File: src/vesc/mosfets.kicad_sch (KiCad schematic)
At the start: 50 parts, among them Q1 NCEP60T20, Q2 NCEP60T20, Q3 NCEP60T20, Q4 NCEP60T20, Q5 NCEP60T20, Q6 NCEP60T20

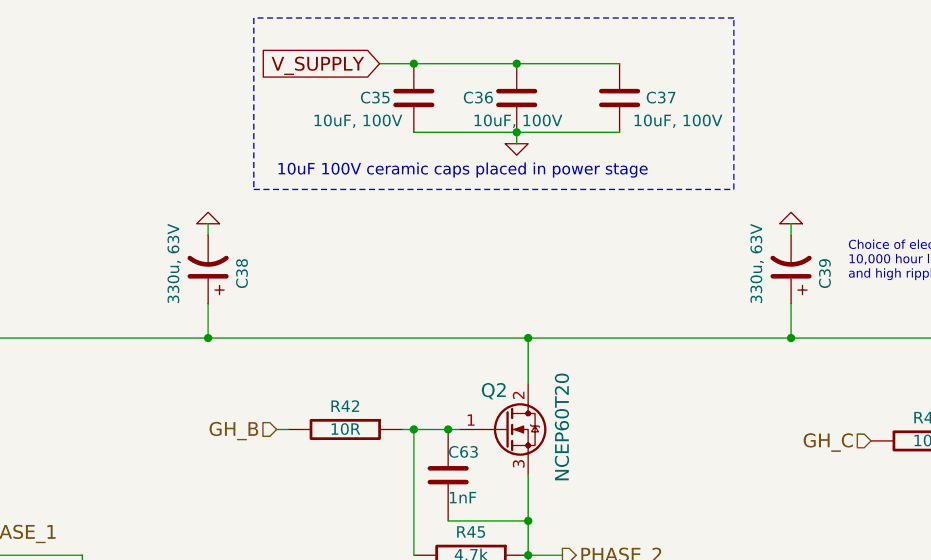
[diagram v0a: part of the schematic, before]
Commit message: replaced 330u electrolytic caps with 270u
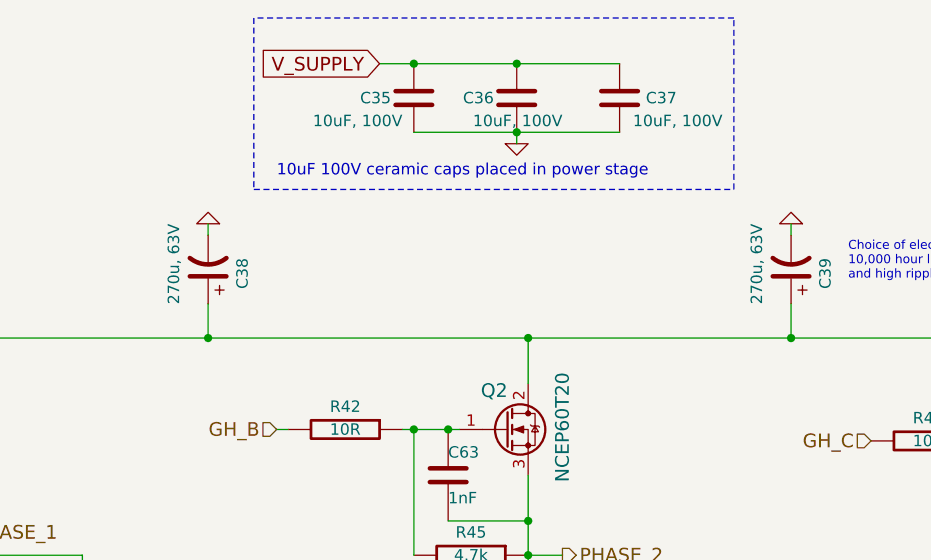
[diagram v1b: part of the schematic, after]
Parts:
- C38, C39: value 330u, 63V -> 270u, 63V
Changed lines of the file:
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@@
 			)
 		)
-		(property "Value" "330u, 63V"
+		(property "Value" "270u, 63V"
 			(at 123.19 58.42 90)
 			(effects
@@
 			)
 		)
-		(property "Value" "330u, 63V"
+		(property "Value" "270u, 63V"
 			(at 187.96 58.42 90)
 			(effects

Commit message: changed power MOSFET capacitor ratings
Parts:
- C35, C36, C37: value 10uF, 100V -> 10uF, 50V
- C40, C41, C42: value 4.7nF, 100V -> 4.7nF, 50V
- C61, C62, C63, C65, C66, C67: value 1nF -> 1nF, 50V
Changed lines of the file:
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@@
 			)
 		)
-		(property "Value" "10uF, 100V"
+		(property "Value" "10uF, 50V"
 			(at 166.37 46.99 0)
 			(effects
@@
 			)
 		)
-		(property "Value" "10uF, 100V"
+		(property "Value" "10uF, 50V"
 			(at 148.59 46.99 0)
 			(effects
@@
 			)
 		)
-		(property "Value" "4.7nF, 100V"
+		(property "Value" "4.7nF, 50V"
 			(at 106.68 107.95 0)
 			(effects
@@
 			)
 		)
-		(property "Value" "4.7nF, 100V"
+		(property "Value" "4.7nF, 50V"
 			(at 172.72 109.22 0)
 			(effects
@@
 			)
 		)
-		(property "Value" "4.7nF, 100V"
+		(property "Value" "4.7nF, 50V"
 			(at 246.38 110.49 0)
 			(effects
@@
 			)
 		)
-		(property "Value" "10uF, 100V"
+		(property "Value" "10uF, 50V"
 			(at 184.15 46.99 0)
 			(effects
@@
 			)
 		)
-		(property "Value" "1nF"
+		(property "Value" "1nF, 50V"
 			(at 86.36 87.63 0)
 			(effects
@@
 			)
 		)
-		(property "Value" "1nF"
+		(property "Value" "1nF, 50V"
 			(at 86.36 111.76 0)
 			(effects
@@
 			)
 		)
-		(property "Value" "1nF"
+		(property "Value" "1nF, 50V"
 			(at 153.67 113.03 0)
 			(effects
@@
 			)
 		)
-		(property "Value" "1nF"
+		(property "Value" "1nF, 50V"
 			(at 153.67 88.9 0)
 			(effects
@@
 			)
 		)
-		(property "Value" "1nF"
+		(property "Value" "1nF, 50V"
 			(at 218.44 90.17 0)
 			(effects
@@
 			)
 		)
-		(property "Value" "1nF"
+		(property "Value" "1nF, 50V"
 			(at 218.44 114.3 0)
 			(effects

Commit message: Fix component values
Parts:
- C35, C36, C37: value 10uF, 50V -> 4u7; footprint Capacitor_SMD:C_2220_5650Metric_Pad1.97x5.40mm_HandSolder -> (none)
- C38, C39: value 270u, 63V -> 270u; footprint w_capacitors:CP_10x20mm_hor_with_model_brd_edge -> (none)
- C40, C41, C42: value 4.7nF, 50V -> 4n7; footprint Capacitor_SMD:C_0805_2012Metric -> (none)
- C61, C62, C63, C65, C66, C67: value 1nF, 50V -> 1n; footprint Capacitor_SMD:C_0603_1608Metric -> (none)
- NT1, NT2, NT3, NT4, NT5, NT6: footprint NetTie:NetTie-2_SMD_Pad0.5mm -> (none)
- Q1, Q2, Q3, Q4, Q5, Q6: footprint shapes3D:TO-220-3_Horizontal_TabUp_no_hole -> (none)
- R33, R37, R39, R41, R42, R43, R47, R48, R49, R53, R54, R55: footprint Resistor_SMD:R_0805_2012Metric -> (none)
- R44, R45, R46, R50, R51, R52: value 4.7k -> 4k7; footprint Resistor_SMD:R_0603_1608Metric -> (none)
- R56, R57, R58, R59, R60, R61: value 0.001R -> 1m; footprint shapes3D:R_2512_Yageo_big_pads -> (none)
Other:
- note added: "C35, C36 and C37 must be 50V rated and placed close to each stage."
- note removed: "10uF 100V ceramic caps placed in power stage"

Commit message: footprints - most resistors and caps, some ICs
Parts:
- C35, C36, C37: footprint (none) -> Capacitor_SMD:C_1210_3225Metric
- C61, C62, C63, C65, C66, C67: footprint (none) -> Capacitor_SMD:C_0402_1005Metric
- R33, R37, R39, R41, R42, R43, R44, R45, R46, R47, R48, R49, R50, R51, R52, R53, R54, R55: footprint (none) -> Resistor_SMD:R_0402_1005Metric
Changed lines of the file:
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@@
 			)
 		)
-		(property "Footprint" ""
+		(property "Footprint" "Capacitor_SMD:C_1210_3225Metric"
 			(at 160.3248 40.64 0)
 			(effects
@@
 			)
 		)
-		(property "Footprint" ""
+		(property "Footprint" "Capacitor_SMD:C_1210_3225Metric"
 			(at 148.8948 40.64 0)
 			(effects
@@
 			)
 		)
-		(property "Footprint" ""
+		(property "Footprint" "Resistor_SMD:R_0402_1005Metric"
 			(at 88.9 119.38 0)
 			(effects
@@
 			)
 		)
-		(property "Footprint" ""
+		(property "Footprint" "Resistor_SMD:R_0402_1005Metric"
 			(at 156.21 119.38 0)
 			(effects
@@
 			)
 		)
-		(property "Footprint" ""
+		(property "Footprint" "Resistor_SMD:R_0402_1005Metric"
 			(at 220.98 120.65 0)
 			(effects
@@
 			)
 		)
-		(property "Footprint" ""
+		(property "Footprint" "Resistor_SMD:R_0402_1005Metric"
 			(at 88.9 92.71 0)
 			(effects
@@
 			)
 		)
-		(property "Footprint" ""
+		(property "Footprint" "Resistor_SMD:R_0402_1005Metric"
 			(at 156.21 95.25 0)
 			(effects
@@
 			)
 		)
-		(property "Footprint" ""
+		(property "Footprint" "Resistor_SMD:R_0402_1005Metric"
 			(at 220.98 95.25 0)
 			(effects
@@
 			)
 		)
-		(property "Footprint" ""
+		(property "Footprint" "Resistor_SMD:R_0402_1005Metric"
 			(at 109.22 120.65 0)
 			(effects
@@
 			)
 		)
-		(property "Footprint" ""
+		(property "Footprint" "Resistor_SMD:R_0402_1005Metric"
 			(at 175.26 121.92 0)
 			(effects
@@
 			)
 		)
-		(property "Footprint" ""
+		(property "Footprint" "Resistor_SMD:R_0402_1005Metric"
 			(at 241.3 123.19 0)
 			(effects
@@
 			)
 		)
-		(property "Footprint" ""
+		(property "Footprint" "Resistor_SMD:R_0402_1005Metric"
 			(at 207.01 82.55 0)
 			(effects
@@
 			)
 		)
-		(property "Footprint" ""
+		(property "Footprint" "Resistor_SMD:R_0402_1005Metric"
 			(at 208.28 106.68 0)
 			(effects
@@
 			)
 		)
-		(property "Footprint" ""
+		(property "Footprint" "Resistor_SMD:R_0402_1005Metric"
 			(at 142.24 81.28 0)
 			(effects
@@
 			)
 		)
-		(property "Footprint" ""
+		(property "Footprint" "Resistor_SMD:R_0402_1005Metric"
 			(at 142.24 105.41 0)
 			(effects
@@
 			)
 		)
-		(property "Footprint" ""
+		(property "Footprint" "Resistor_SMD:R_0402_1005Metric"
 			(at 71.12 104.14 0)
 			(effects
@@
 			)
 		)
-		(property "Footprint" ""
+		(property "Footprint" "Resistor_SMD:R_0402_1005Metric"
 			(at 71.12 80.01 0)
 			(effects
@@
 			)
 		)
-		(property "Footprint" ""
+		(property "Footprint" "Capacitor_SMD:C_1210_3225Metric"
 			(at 171.7548 40.64 0)
 			(effects
@@
 			)
 		)
-		(property "Footprint" ""
+		(property "Footprint" "Resistor_SMD:R_0402_1005Metric"
 			(at 116.84 120.65 0)
 			(effects
@@
 			)
 		)
-		(property "Footprint" ""
+		(property "Footprint" "Resistor_SMD:R_0402_1005Metric"
 			(at 182.88 121.92 0)
 			(effects
@@
 			)
 		)
-		(property "Footprint" ""
+		(property "Footprint" "Resistor_SMD:R_0402_1005Metric"
 			(at 248.92 123.19 0)
 			(effects
@@
 			)
 		)
-		(property "Footprint" ""
+		(property "Footprint" "Capacitor_SMD:C_0402_1005Metric"
 			(at 86.36 85.09 0)
 			(effects
@@
 			)
 		)
-		(property "Footprint" ""
+		(property "Footprint" "Capacitor_SMD:C_0402_1005Metric"
 			(at 86.36 109.22 0)
 			(effects
@@
 			)
 		)
-		(property "Footprint" ""
+		(property "Footprint" "Capacitor_SMD:C_0402_1005Metric"
 			(at 153.67 110.49 0)
 			(effects
@@
 			)
 		)
-		(property "Footprint" ""
+		(property "Footprint" "Capacitor_SMD:C_0402_1005Metric"
 			(at 153.67 86.36 0)
 			(effects
@@
 			)
 		)
-		(property "Footprint" ""
+		(property "Footprint" "Capacitor_SMD:C_0402_1005Metric"
 			(at 218.44 87.63 0)
 			(effects
@@
 			)
 		)
-		(property "Footprint" ""
+		(property "Footprint" "Capacitor_SMD:C_0402_1005Metric"
 			(at 218.44 111.76 0)
 			(effects

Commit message: footprints for remaining caps, resistors, diodes, MOSFETs. and ICs
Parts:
- C38, C39: footprint (none) -> Capacitor_SMD:CP_Elec_10x10
- C40, C41, C42: value 4n7 -> 3n3; footprint (none) -> Capacitor_SMD:C_0402_1005Metric
- Q1, Q2, Q3, Q4, Q5, Q6: footprint (none) -> Package_TO_SOT_THT:TO-220-3_Horizontal_TabUp
- R56, R57, R58, R59, R60, R61: footprint (none) -> Resistor_SMD:R_2512_6332Metric
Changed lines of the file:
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@@
 			)
 		)
-		(property "Footprint" ""
+		(property "Footprint" "Package_TO_SOT_THT:TO-220-3_Horizontal_TabUp"
 			(at 92.71 80.01 0)
 			(effects
@@
 			)
 		)
-		(property "Footprint" ""
+		(property "Footprint" "Package_TO_SOT_THT:TO-220-3_Horizontal_TabUp"
 			(at 92.71 104.14 0)
 			(effects
@@
 			)
 		)
-		(property "Footprint" ""
+		(property "Footprint" "Package_TO_SOT_THT:TO-220-3_Horizontal_TabUp"
 			(at 160.02 105.41 0)
 			(effects
@@
 			)
 		)
-		(property "Footprint" ""
+		(property "Footprint" "Package_TO_SOT_THT:TO-220-3_Horizontal_TabUp"
 			(at 160.02 81.28 0)
 			(effects
@@
 			)
 		)
-		(property "Footprint" ""
+		(property "Footprint" "Package_TO_SOT_THT:TO-220-3_Horizontal_TabUp"
 			(at 224.79 82.55 0)
 			(effects
@@
 			)
 		)
-		(property "Footprint" ""
+		(property "Footprint" "Package_TO_SOT_THT:TO-220-3_Horizontal_TabUp"
 			(at 224.79 106.68 0)
 			(effects
@@
 			)
 		)
-		(property "Footprint" ""
+		(property "Footprint" "Resistor_SMD:R_2512_6332Metric"
 			(at 95.25 134.62 0)
 			(effects
@@
 			)
 		)
-		(property "Footprint" ""
+		(property "Footprint" "Resistor_SMD:R_2512_6332Metric"
 			(at 162.56 135.89 0)
 			(effects
@@
 			)
 		)
-		(property "Footprint" ""
+		(property "Footprint" "Resistor_SMD:R_2512_6332Metric"
 			(at 227.33 137.16 0)
 			(effects
@@
 			)
 		)
-		(property "Footprint" ""
+		(property "Footprint" "Capacitor_SMD:CP_Elec_10x10"
 			(at 127 63.5 0)
 			(effects
@@
 			)
 		)
-		(property "Value" "4n7"
+		(property "Value" "3n3"
 			(at 106.68 107.95 0)
 			(effects
@@
 			)
 		)
-		(property "Footprint" ""
+		(property "Footprint" "Capacitor_SMD:C_0402_1005Metric"
 			(at 113.03 105.41 0)
 			(effects
@@
 			)
 		)
-		(property "Value" "4n7"
+		(property "Value" "3n3"
 			(at 172.72 109.22 0)
 			(effects
@@
 			)
 		)
-		(property "Footprint" ""
+		(property "Footprint" "Capacitor_SMD:C_0402_1005Metric"
 			(at 179.07 106.68 0)
 			(effects
@@
 			)
 		)
-		(property "Value" "4n7"
+		(property "Value" "3n3"
 			(at 246.38 110.49 0)
 			(effects
@@
 			)
 		)
-		(property "Footprint" ""
+		(property "Footprint" "Capacitor_SMD:C_0402_1005Metric"
 			(at 245.11 107.95 0)
 			(effects
@@
 			)
 		)
-		(property "Footprint" ""
+		(property "Footprint" "Capacitor_SMD:CP_Elec_10x10"
 			(at 191.77 63.5 0)
 			(effects
@@
 			)
 		)
-		(property "Footprint" ""
+		(property "Footprint" "Resistor_SMD:R_2512_6332Metric"
 			(at 168.91 135.89 0)
 			(effects
@@
 			)
 		)
-		(property "Footprint" ""
+		(property "Footprint" "Resistor_SMD:R_2512_6332Metric"
 			(at 101.6 134.62 0)
 			(effects
@@
 			)
 		)
-		(property "Footprint" ""
+		(property "Footprint" "Resistor_SMD:R_2512_6332Metric"
 			(at 233.68 137.16 0)
 			(effects

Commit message: old logos, net ties
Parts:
- NT1, NT2, NT3, NT4, NT5, NT6: footprint (none) -> NetTie:NetTie-2_SMD_Pad0.5mm
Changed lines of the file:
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@@
 			)
 		)
-		(property "Footprint" ""
+		(property "Footprint" "NetTie:NetTie-2_SMD_Pad0.5mm"
 			(at 87.63 129.54 0)
 			(effects
@@
 			)
 		)
-		(property "Footprint" ""
+		(property "Footprint" "NetTie:NetTie-2_SMD_Pad0.5mm"
 			(at 87.63 139.7 0)
 			(effects
@@
 			)
 		)
-		(property "Footprint" ""
+		(property "Footprint" "NetTie:NetTie-2_SMD_Pad0.5mm"
 			(at 156.21 130.81 0)
 			(effects
@@
 			)
 		)
-		(property "Footprint" ""
+		(property "Footprint" "NetTie:NetTie-2_SMD_Pad0.5mm"
 			(at 156.21 142.24 0)
 			(effects
@@
 			)
 		)
-		(property "Footprint" ""
+		(property "Footprint" "NetTie:NetTie-2_SMD_Pad0.5mm"
 			(at 220.98 132.08 0)
 			(effects
@@
 			)
 		)
-		(property "Footprint" ""
+		(property "Footprint" "NetTie:NetTie-2_SMD_Pad0.5mm"
 			(at 220.98 142.24 0)
 			(effects

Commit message: component placement
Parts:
- removed NT1, NT2, NT3, NT4, NT5, NT6: Net-Tie_2, NetTie:NetTie-2_SMD_Pad0.5mm, symbol Device:Net-Tie_2
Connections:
- net H1_LOW is gone; now on net SNA: C62.2, Q4.3 (S), R50.2, R56.2, R57.2
- net H2_LOW is gone; now on net SNB: C65.2, Q5.3 (S), R51.1, R58.2, R59.2
- net H3_LOW is gone; now on net SNC: C67.2, Q6.3 (S), R52.1, R60.2, R61.2

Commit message: MOSFET routing almost
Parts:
- Q1, Q2, Q3, Q4, Q5, Q6: footprint Package_TO_SOT_THT:TO-220-3_Horizontal_TabUp -> Bluesat:TO-220-3-heatsink-pad-tabdown
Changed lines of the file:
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@@
-	(wire
-		(pts
-			(xy 149.86 142.24) (xy 162.56 142.24)
-		)
-		(stroke
-			(width 0)
-			(type default)
-		)
-	)
 	(wire
 		(pts
@@
 	(wire
 		(pts
-			(xy 214.63 142.24) (xy 227.33 142.24)
-		)
-		(stroke
-			(width 0)
-			(type default)
-		)
-	)
-	(wire
-		(pts
 			(xy 227.33 146.05) (xy 227.33 142.24)
 		)
@@
 	(wire
 		(pts
-			(xy 81.28 139.7) (xy 95.25 139.7)
-		)
-		(stroke
-			(width 0)
-			(type default)
-		)
-	)
-	(wire
-		(pts
 			(xy 162.56 119.38) (xy 162.56 124.46)
 		)
@@
 			(width 0)
 			(type default)
-		)
-	)
-	(global_label "SPC"
-		(shape input)
-		(at 214.63 142.24 180)
-		(effects
-			(font
-				(size 1.524 1.524)
-			)
-			(justify right)
-		)
-		(property "Intersheetrefs" "${INTERSHEET_REFS}"
-			(at 214.63 142.24 0)
-			(effects
-				(font
-					(size 1.27 1.27)
-				)
-				(hide yes)
-			)
 		)
 	)
@@
 		(property "Intersheetrefs" "${INTERSHEET_REFS}"
 			(at 81.28 129.54 0)
-			(effects
-				(font
-					(size 1.27 1.27)
-				)
-				(hide yes)
-			)
-		)
-	)
-	(global_label "SPA"
-		(shape input)
-		(at 81.28 139.7 180)
-		(effects
-			(font
-				(size 1.524 1.524)
-			)
-			(justify right)
-		)
-		(property "Intersheetrefs" "${INTERSHEET_REFS}"
-			(at 81.28 139.7 0)
-			(effects
-				(font
-					(size 1.27 1.27)
-				)
-				(hide yes)
-			)
-		)
-	)
-	(global_label "SPB"
-		(shape input)
-		(at 149.86 142.24 180)
-		(effects
-			(font
-				(size 1.524 1.524)
-			)
-			(justify right)
-		)
-		(property "Intersheetrefs" "${INTERSHEET_REFS}"
-			(at 149.86 142.24 0)
 			(effects
 				(font
@@
 			)
 		)
-		(property "Footprint" "Package_TO_SOT_THT:TO-220-3_Horizontal_TabUp"
+		(property "Footprint" "Bluesat:TO-220-3-heatsink-pad-tabdown"
 			(at 92.71 80.01 0)
 			(effects
@@
 			)
 		)
-		(property "Footprint" "Package_TO_SOT_THT:TO-220-3_Horizontal_TabUp"
+		(property "Footprint" "Bluesat:TO-220-3-heatsink-pad-tabdown"
 			(at 92.71 104.14 0)
 			(effects
@@
 			)
 		)
-		(property "Footprint" "Package_TO_SOT_THT:TO-220-3_Horizontal_TabUp"
+		(property "Footprint" "Bluesat:TO-220-3-heatsink-pad-tabdown"
 			(at 160.02 105.41 0)
 			(effects
@@
 			)
 		)
-		(property "Footprint" "Package_TO_SOT_THT:TO-220-3_Horizontal_TabUp"
+		(property "Footprint" "Bluesat:TO-220-3-heatsink-pad-tabdown"
 			(at 160.02 81.28 0)
 			(effects
@@
 			)
 		)
-		(property "Footprint" "Package_TO_SOT_THT:TO-220-3_Horizontal_TabUp"
+		(property "Footprint" "Bluesat:TO-220-3-heatsink-pad-tabdown"
 			(at 224.79 82.55 0)
 			(effects
@@
 			)
 		)
-		(property "Footprint" "Package_TO_SOT_THT:TO-220-3_Horizontal_TabUp"
+		(property "Footprint" "Bluesat:TO-220-3-heatsink-pad-tabdown"
 			(at 224.79 106.68 0)
 			(effects
